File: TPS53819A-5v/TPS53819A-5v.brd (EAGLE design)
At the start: 74 x 19 mm, 27 parts, among them IC1 TPS53819A

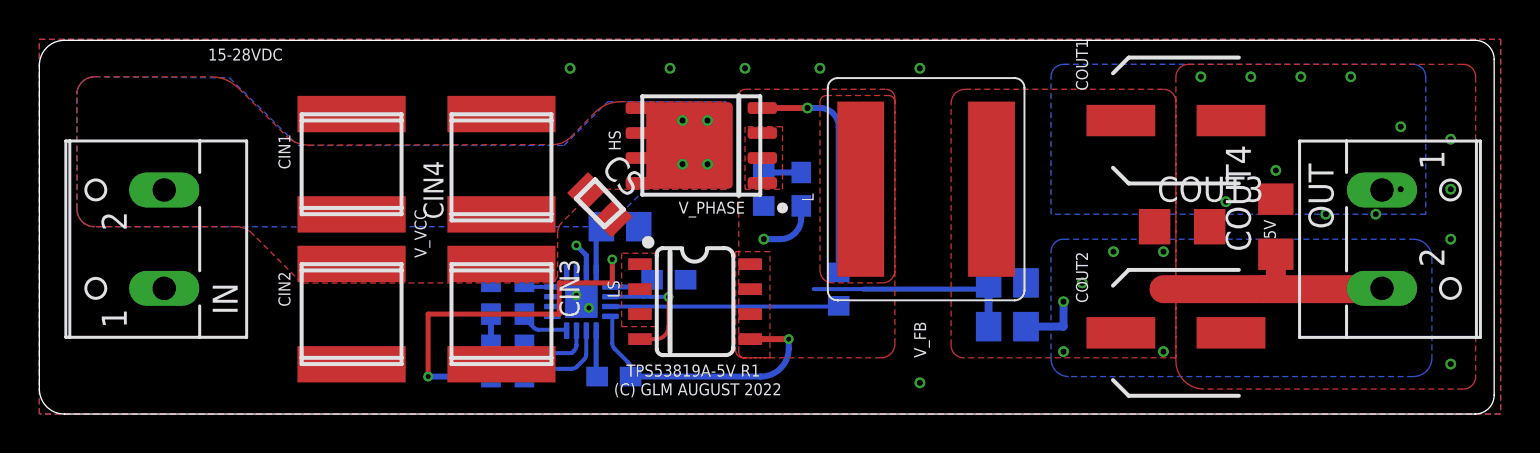
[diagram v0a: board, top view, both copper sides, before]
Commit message: made progress on routing, missing i2c connector still
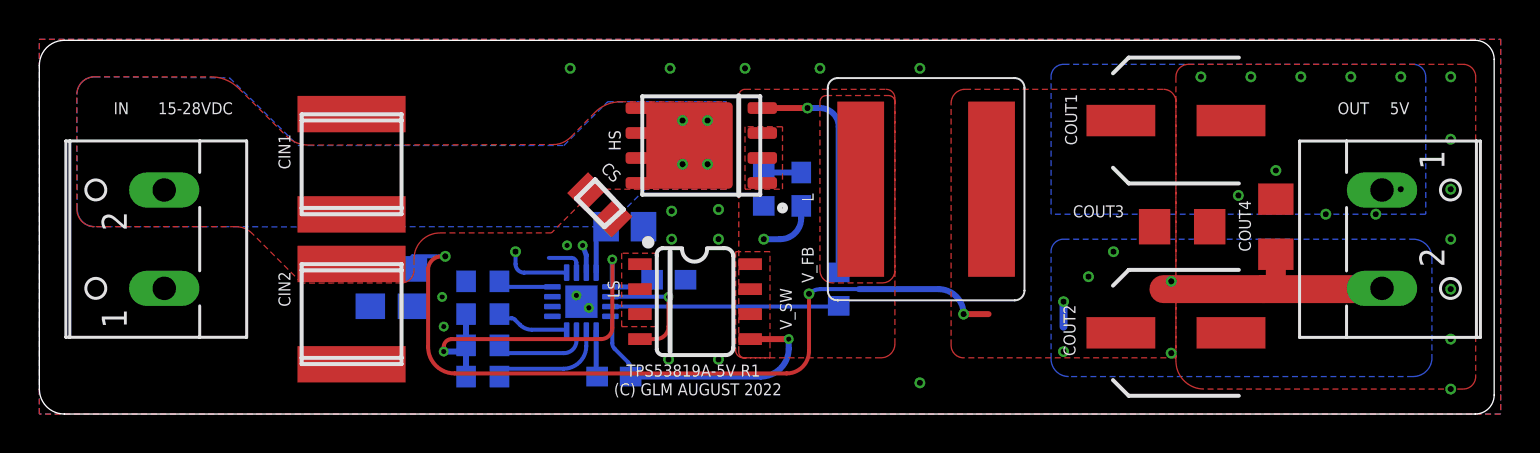
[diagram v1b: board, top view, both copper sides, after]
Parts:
- removed CIN3, CIN4: 33u, rcl:C2220K
- moved RFB2 32.4 mm to (27.0, 6.43), turned to 90 degrees
- moved RFB1 30.3 mm to (29.1, 6.43), turned to 90 degrees
- moved R1 1.27 mm to (32.7, 1.91)
- moved R2 1.27 mm to (32.7, 3.49)
- moved R3 1.27 mm to (32.7, 5.08)
- moved R4 1.27 mm to (32.7, 6.75)
- moved CVDD 0.24 mm to (39.9, 9.53)
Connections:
- net GND: no longer CIN3.2, CIN4.2
- net VDD: no longer CIN3.1, CIN4.1
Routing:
- net VOUT: track 16.7 -> 58.6 mm, vias 6 -> 10
- net FB: track 11.4 -> 2.01 mm
- net VREG: track 26.0 -> 21.6 mm
- net TRIP: track 1.70 -> 2.97 mm
- net ADDR: track 2.60 -> 3.82 mm
- net PGOOD: track 3.78 -> 4.85 mm
- net EN: track 4.86 -> 5.84 mm
- net GND: track 1.59 -> 1.42 mm, vias 23 -> 35
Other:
- board text added: "V_SW"
